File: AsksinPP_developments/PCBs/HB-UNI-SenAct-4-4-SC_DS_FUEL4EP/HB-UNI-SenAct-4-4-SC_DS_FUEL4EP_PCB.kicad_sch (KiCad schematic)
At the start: 54 parts, among them J1 5V supply, J10 charge, J2 4x Push Buttons, J3 4x Relais, J4 5x LEDs, J5 ISP Programmer, J6 Accumulator, J7 GND, J8 VCC, Q1 IRLU024N, Q2 BD238, Q4 IRF9Z34N, Q5 MCP1702-2802E_TO, SW1 SW_Push, SW2 SW_Push

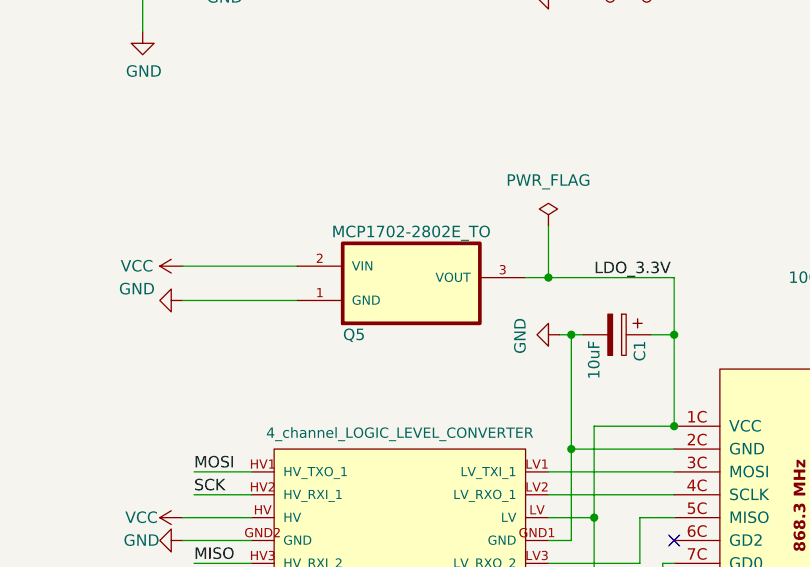
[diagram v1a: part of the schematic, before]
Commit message: HM-LC-Bl1-FM_FUEL4EP and HB-UNI-SenAct-4-4-SC_DS_FUEL4EP: fix of MCP1702 from 2.8V to 3.3V version
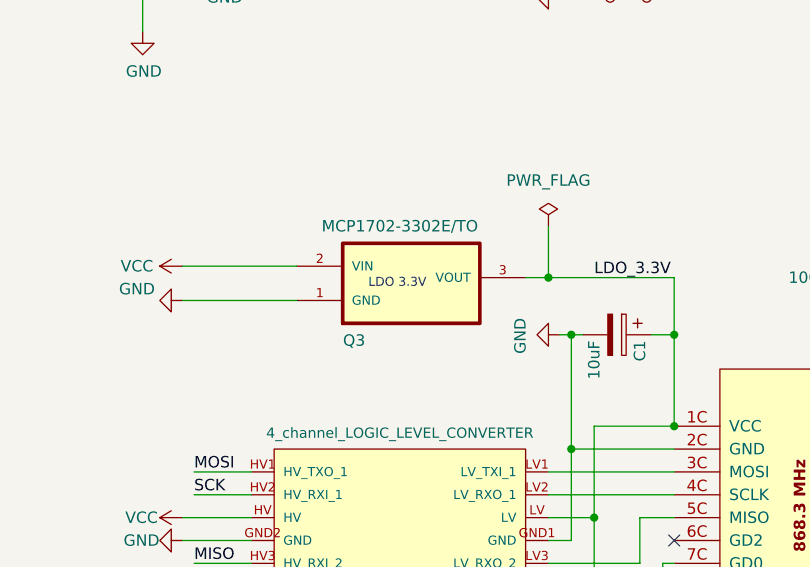
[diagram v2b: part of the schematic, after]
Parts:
- removed Q5: MCP1702-2802E_TO, FUEL4EP:TO127P254X533-3, symbol FUEL4EP:MCP1702-2802E_TO
- added Q3: MCP1702-3302E/TO, TO127P254X533-3, symbol FUEL4EP:MCP1702-3302E/TO
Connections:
- net GND: now also Q3.1 (GND)
- net LDO_3.3V: now also Q3.3 (VOUT)
- net VCC: now also Q3.2 (VIN)
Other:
- note added: "LDO 3.3V"
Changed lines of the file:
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@@
   (title_block
     (title "SenAct-4-4-SC_FUEL4EP_PCB")
-    (date "2023-07-22")
-    (rev "1.4")
+    (date "2023-07-28")
+    (rev "1.5")
     (company "FUEL4EP")
     (comment 1 "3x Schalter Schaltaktor AsksinPP PCB für Netzfreischalter")
@@
   (text "Monitor\n" (at 102.235 105.41 0)
     (effects (font (size 1.27 1.27)) (justify left bottom))
+  )
+  (text "LDO 3.3V\n" (at 59.9946 145.4326 0)
+    (effects (font (size 1 1)) (justify left bottom))
   )
   (text "Heating\n" (at 265.43 60.96 0)
@@
     )
   )
-  (symbol (lib_id "FUEL4EP:MCP1702-2802E_TO") (at 57.15 140.335 0) (unit 1)
-    (in_bom yes) (on_board yes)
-    (property "Reference" "Q5" (id 0) (at 58.42 150.495 0))
-    (property "Value" "MCP1702-2802E_TO" (id 1) (at 64.77 139.065 0))
-    (property "Footprint" "FUEL4EP:TO127P254X533-3" (id 2) (at 57.15 140.335 0)
-      (effects (font (size 1.27 1.27)) (justify left bottom) hide)
-    )
-    (property "Datasheet" "" (id 3) (at 57.15 140.335 0)
-      (effects (font (size 1.27 1.27)) (justify left bottom) hide)
-    )
-    (property "OC_FARNELL" "1331485" (id 4) (at 57.15 140.335 0)
-      (effects (font (size 1.27 1.27)) (justify left bottom) hide)
-    )
-    (property "SUPPLIER" "Microchip" (id 5) (at 57.15 140.335 0)
-      (effects (font (size 1.27 1.27)) (justify left bottom) hide)
-    )
-    (property "MPN" "MCP1702-2802E/TO" (id 6) (at 57.15 140.335 0)
-      (effects (font (size 1.27 1.27)) (justify left bottom) hide)
-    )
-    (property "PACKAGE" "TO-92" (id 7) (at 57.15 140.335 0)
-      (effects (font (size 1.27 1.27)) (justify left bottom) hide)
-    )
-    (property "OC_NEWARK" "34M7419" (id 8) (at 57.15 140.335 0)
-      (effects (font (size 1.27 1.27)) (justify left bottom) hide)
-    )
-    (pin "1")
-    (pin "2")
-    (pin "3")
-  )
   (symbol (lib_id "FUEL4EP:IRF9Z34N") (at 198.12 32.385 90) (unit 1)
     (in_bom yes) (on_board yes)
@@
     (pin "2")
   )
+  (symbol (lib_id "FUEL4EP:MCP1702-3302E{slash}TO") (at 57.15 140.335 0) (unit 1)
+    (in_bom yes) (on_board yes)
+    (property "Reference" "Q3" (id 0) (at 58.42 151.13 0))
+    (property "Value" "MCP1702-3302E/TO" (id 1) (at 63.5 138.43 0))
+    (property "Footprint" "TO127P254X533-3" (id 2) (at 63.5 134.62 0)
+      (effects (font (size 1.27 1.27)) (justify left bottom) hide)
+    )
+    (property "Datasheet" "https://ww1.microchip.com/downloads/en/DeviceDoc/22008E.pdf" (id 3) (at 63.5 139.7 0)
+      (effects (font (size 1.27 1.27)) (justify left bottom) hide)
+    )
+    (property "SUPPLIER" "Microchip" (id 4) (at 63.5 137.16 0)
+      (effects (font (size 1.27 1.27)) (justify left bottom) hide)
+    )
+    (property "PACKAGE" "TO-92" (id 5) (at 63.5 132.08 0)
+      (effects (font (size 1.27 1.27)) (justify left bottom) hide)
+    )
+    (pin "1")
+    (pin "2")
+    (pin "3")
+  )
   (symbol (lib_id "power:PWR_FLAG") (at 143.51 18.415 0) (unit 1)
     (in_bom yes) (on_board yes)
@@
       (reference "Q2") (unit 1) (value "BD238") (footprint "Package_TO_SOT_THT:TO-126-3_Vertical")
     )
+    (path "/053dd794-1fc5-42b8-96b0-9604d84c4640"
+      (reference "Q3") (unit 1) (value "MCP1702-3302E/TO") (footprint "TO127P254X533-3")
+    )
     (path "/00000000-0000-0000-0000-0000619ef6e1"
       (reference "Q4") (unit 1) (value "IRF9Z34N") (footprint "FUEL4EP:TO220V")
     )
-    (path "/00000000-0000-0000-0000-0000619a7cde"
-      (reference "Q5") (unit 1) (value "MCP1702-2802E_TO") (footprint "FUEL4EP:TO127P254X533-3")
-    )
     (path "/00000000-0000-0000-0000-00005abe25c7"

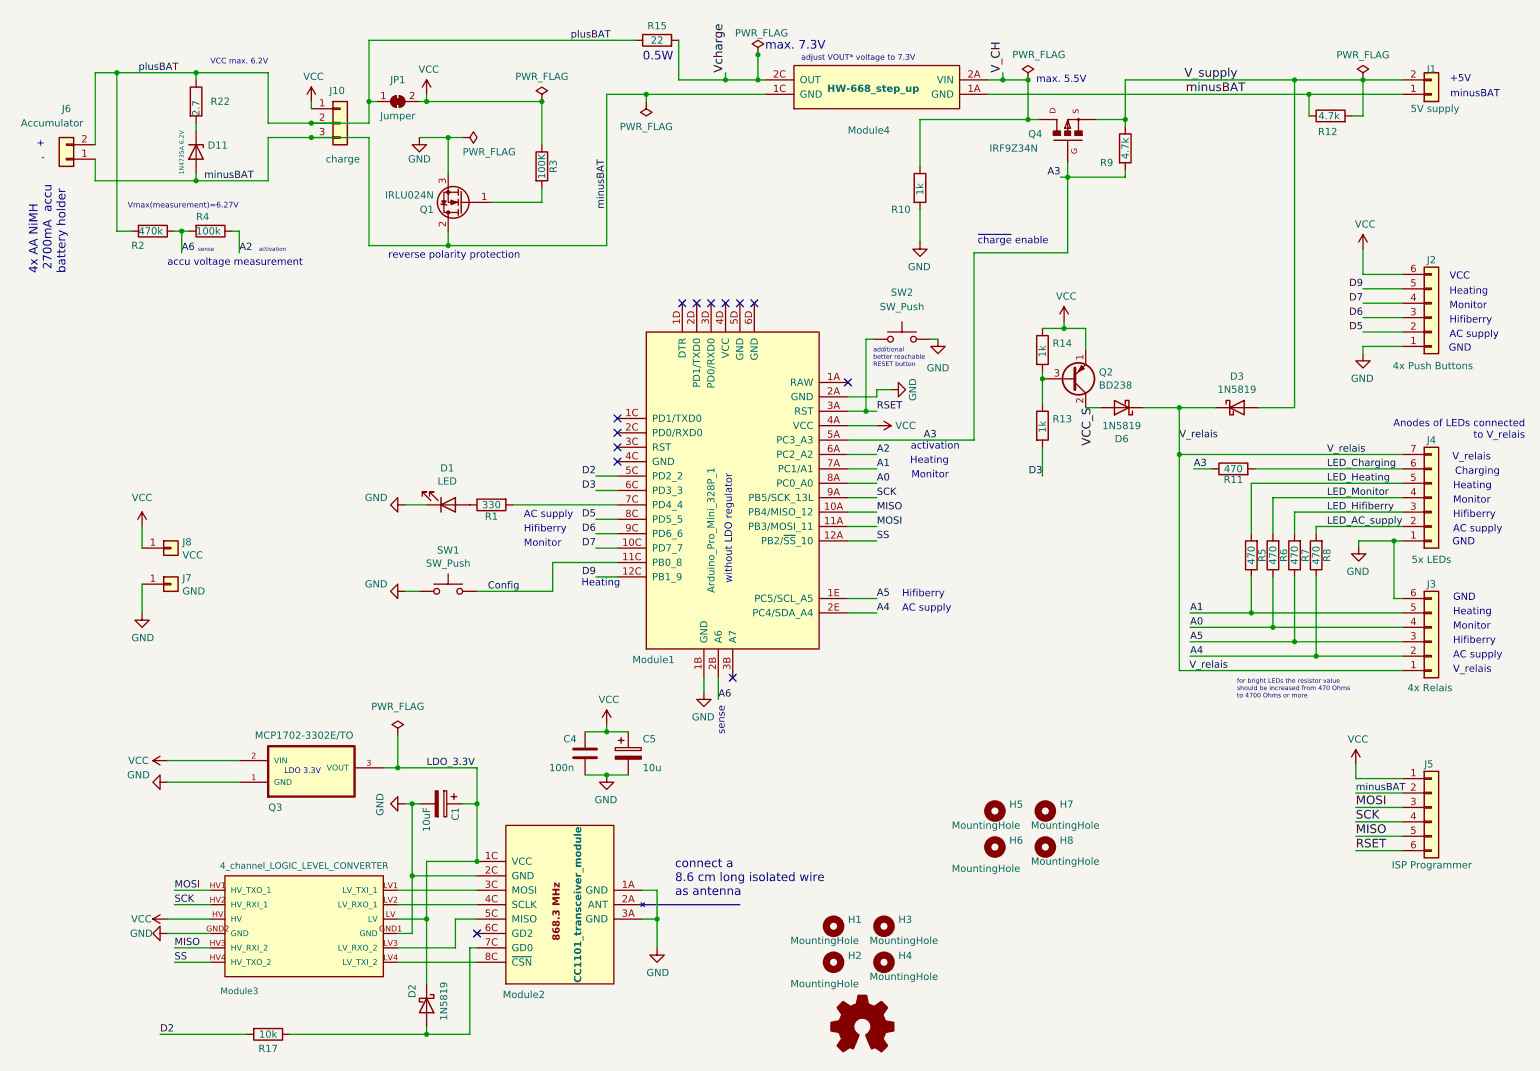
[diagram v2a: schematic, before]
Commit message: PCBs/HB-UNI-SenAct-4-4-SC_DS_FUEL4EP: migration to KiCAD 8
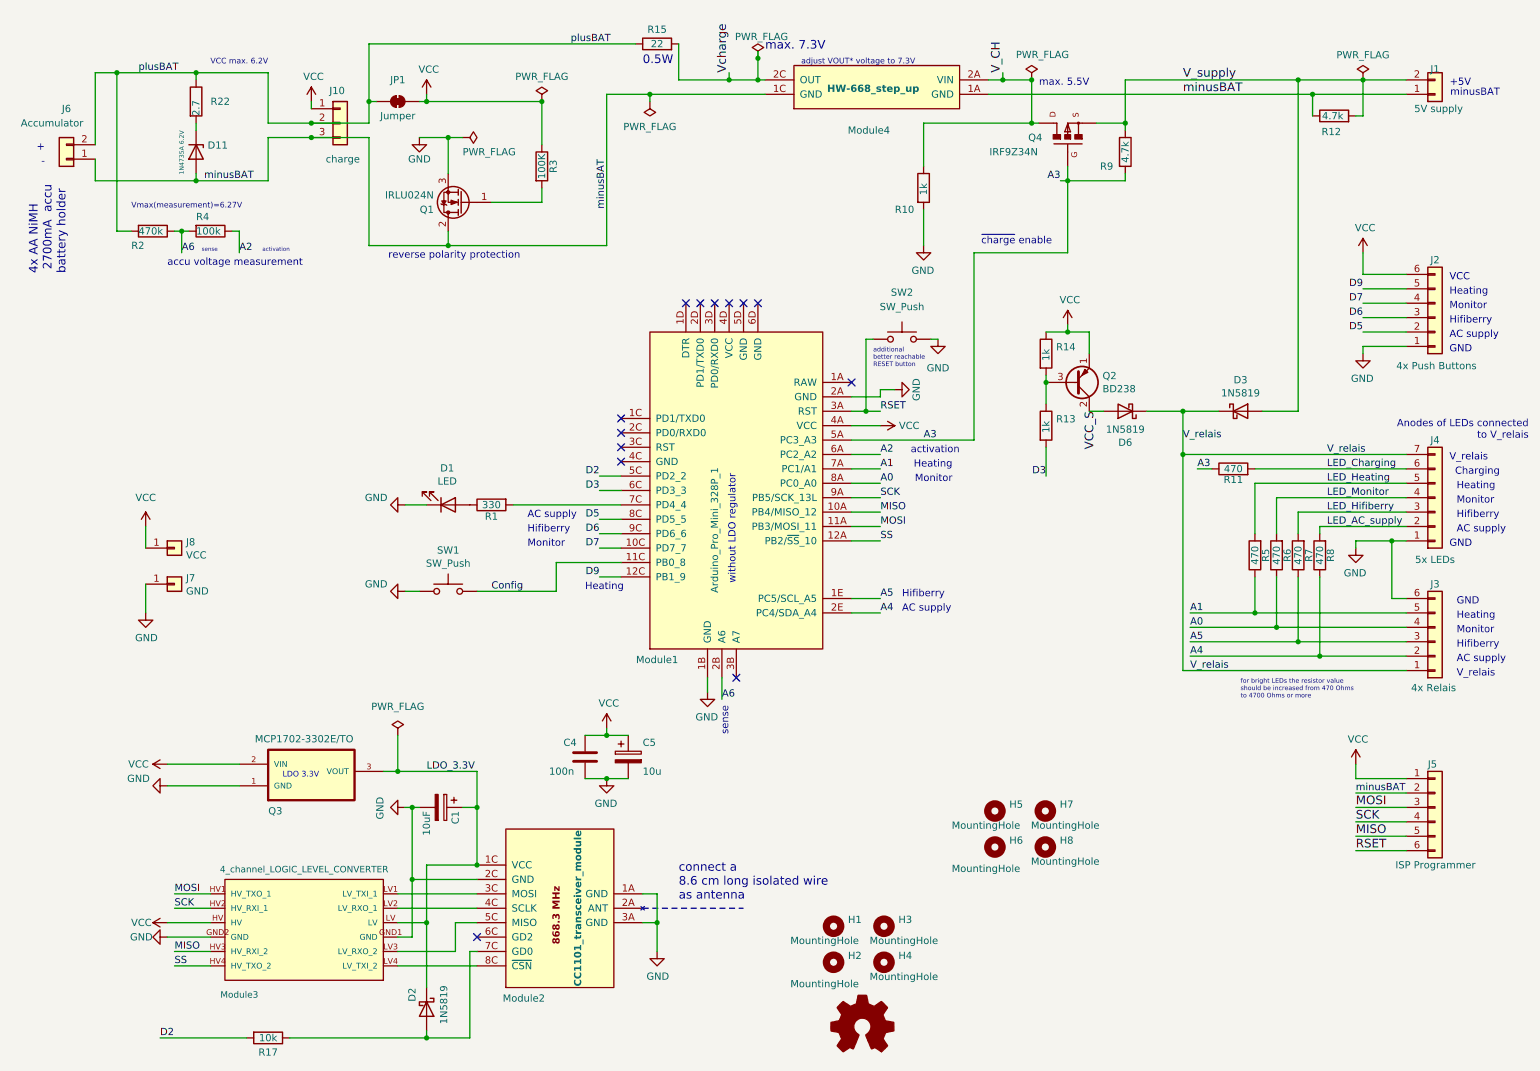
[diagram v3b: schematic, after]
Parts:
- Q3: footprint TO127P254X533-3 -> FUEL4EP:TO127P254X533-3; symbol FUEL4EP:MCP1702-3302E/TO -> FUEL4EP:MCP1702-3302E/TO
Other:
- moved on the sheet: C1, C4, C5, D2, D3, D6, J1, J2, J3, J4, J5, J7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
